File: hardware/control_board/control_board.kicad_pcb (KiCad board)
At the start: 2 copper layers, 286 x 99.4 mm, 124 parts, among them IC1 24LC512, IC10 ATMEGA644p, IC2 74HC165, IC3 74HC165, IC4 4051, IC5 4051, IC6 4051, IC7 4051, IC8 74HC595, IC9 74HC165, J1 Conn_01x08, J2 Conn_01x06, Q1 20MHz, SW1 Encoder, U1 AVR ISP, X1 MIDI, X2 MIDI

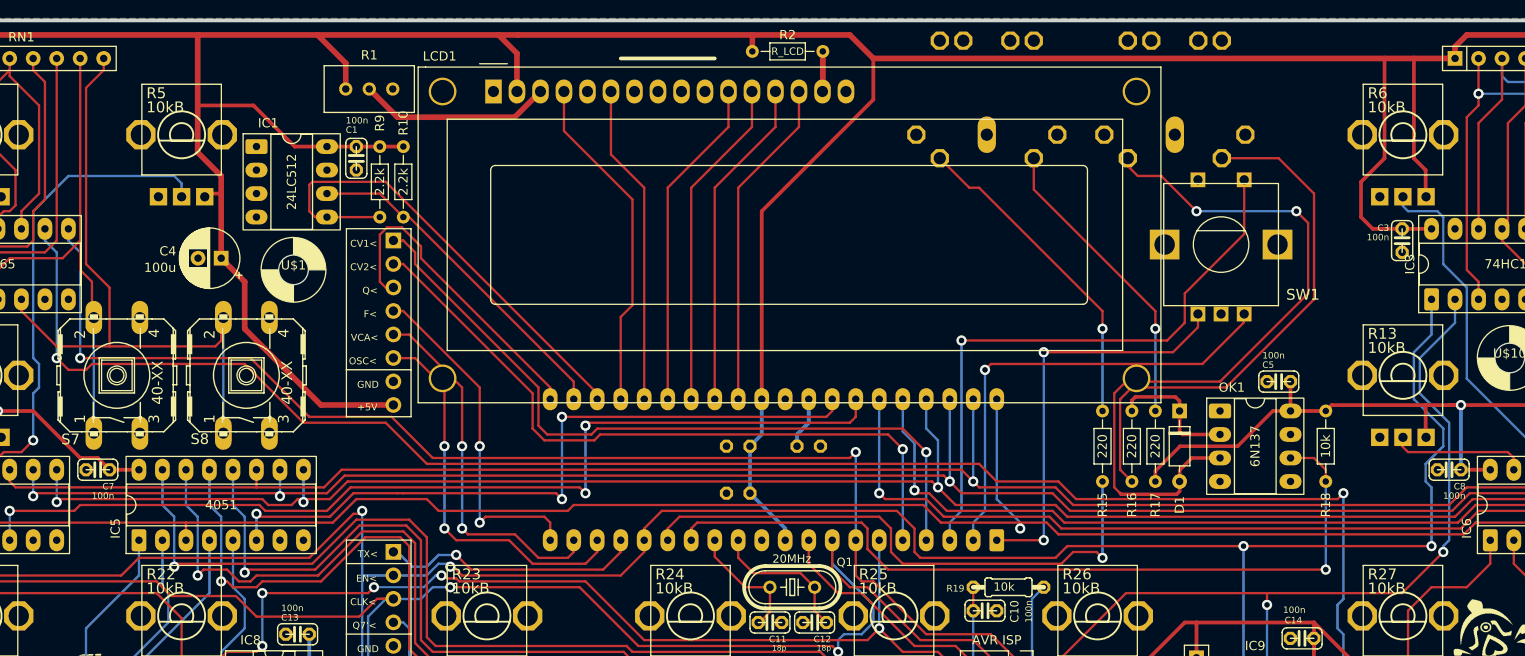
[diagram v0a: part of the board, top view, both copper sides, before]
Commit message: move midi components to daughterboard
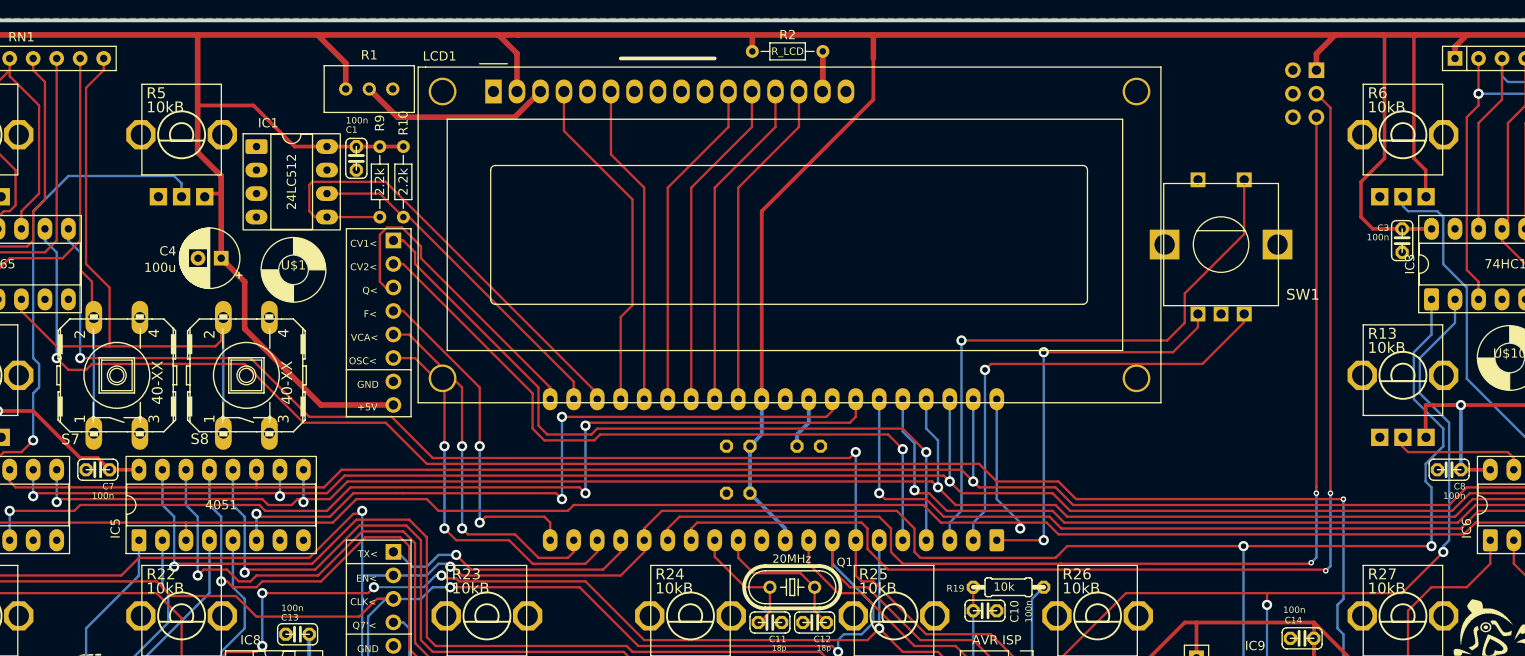
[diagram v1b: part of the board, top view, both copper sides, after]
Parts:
- removed C5: 100n, shruthi_control_board_xt_v03:C025-024X044
- removed D1: 1N4148, Diode_THT:D_DO-35_SOD27_P7.62mm_Horizontal
- removed OK1: 6N137, Package_DIP:DIP-8_W7.62mm_Socket_LongPads
- removed R15, R16, R17: 220, Resistor_THT:R_Axial_DIN0204_L3.6mm_D1.6mm_P7.62mm_Horizontal
- removed R18: 10k, Resistor_THT:R_Axial_DIN0204_L3.6mm_D1.6mm_P7.62mm_Horizontal
- removed X1, X2: MIDI, shruthi_control_board_xt_v03:MAB5SH
- added J3: MIDI_IO, Connector_PinHeader_2.54mm:PinHeader_2x03_P2.54mm_Vertical, B.Cu at (270.5, 99.1)
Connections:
- net Net-(LCD1-VO) renamed /buttons/VO
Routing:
- net Net-(D1-A): track 80.8 -> 0.00 mm, vias 2 -> 0
- net /mcu/MIDI_TX: track 61.4 -> 123.5 mm, vias 1 -> 2
- net Net-(R16-Pad1): track 57.8 -> 0.00 mm
- net /mcu/MIDI_RX: track 88.7 -> 126.0 mm, vias 1 -> 2
- net Net-(R15-Pad1): track 35.2 -> 0.00 mm, vias 1 -> 0
- net Net-(R17-Pad1): track 32.8 -> 0.00 mm, vias 1 -> 0
- net VCC: track 1504.5 -> 1480.7 mm
- net Net-(D1-K): track 14.4 -> 0.00 mm
- net /buttons/INPUT_CHAIN_2: track 200.1 -> 199.2 mm
